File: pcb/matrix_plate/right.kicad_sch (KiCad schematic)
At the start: 39 parts

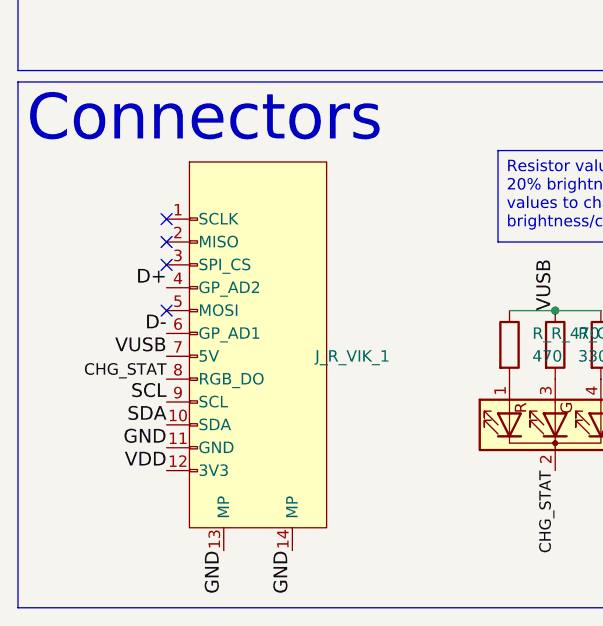
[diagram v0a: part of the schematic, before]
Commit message: Update KiCAD projects to use new library locations.
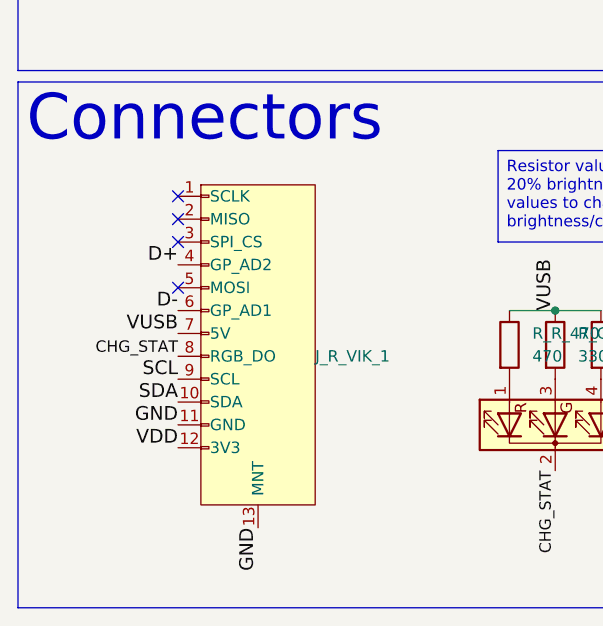
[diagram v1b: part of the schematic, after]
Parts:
- J_R_VIK_1: footprint vik:vik-module-connector-horizontal -> footprints:vik-module-connector-horizontal
- S_R_00, S_R_01, S_R_02, S_R_03, S_R_04, S_R_10, S_R_11, S_R_12, S_R_13, S_R_14, S_R_15, S_R_20, S_R_21, S_R_22, S_R_23, S_R_24, S_R_25, S_R_31, S_R_32, S_R_33, S_R_34, S_R_35: footprint key-switches:SW_GLP_Kailh_Choc_V1V2_HotSwap_PTH -> footprints:SW_GLP_Kailh_Choc_V1V2_HotSwap_PTH
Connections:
- net GND: no longer J_R_VIK_1.14 (MP)
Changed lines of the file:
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@@
 	)
 	(no_connect
-		(at 29.21 180.34)
+		(at 30.48 177.8)
 	)
 	(no_connect
@@
 	)
 	(no_connect
-		(at 29.21 187.96)
+		(at 30.48 185.42)
 	)
 	(no_connect
@@
 	)
 	(no_connect
-		(at 29.21 177.8)
+		(at 30.48 175.26)
 	)
 	(no_connect
@@
 	)
 	(no_connect
-		(at 29.21 182.88)
+		(at 30.48 180.34)
 	)
 	(wire
@@
 	)
 	(label "D+"
-		(at 29.21 185.42 180)
+		(at 30.48 182.88 180)
 		(effects
 			(font
@@
 	)
 	(label "CHG_STAT"
-		(at 29.21 195.58 180)
+		(at 30.48 193.04 180)
 		(effects
 			(font
@@
 	)
 	(label "SDA"
-		(at 29.21 200.66 180)
+		(at 30.48 198.12 180)
 		(effects
 			(font
@@
 	)
 	(label "VUSB"
-		(at 29.21 193.04 180)
+		(at 30.48 190.5 180)
 		(effects
 			(font
@@
 	)
 	(label "GND"
-		(at 29.21 203.2 180)
+		(at 30.48 200.66 180)
 		(effects
 			(font
@@
 	)
 	(label "GND"
-		(at 35.56 214.63 270)
+		(at 39.37 212.09 270)
 		(effects
 			(font
@@
 		)
 	)
-	(label "GND"
-		(at 43.18 214.63 270)
-		(effects
-			(font
-				(size 1.524 1.524)
-			)
-			(justify right bottom)
-		)
-	)
 	(label "D-"
 		(at 308.61 45.72 0)
@@
 	)
 	(label "VDD"
-		(at 29.21 205.74 180)
+		(at 30.48 203.2 180)
 		(effects
 			(font
@@
 	)
 	(label "SCL"
-		(at 29.21 198.12 180)
+		(at 30.48 195.58 180)
 		(effects
 			(font
@@
 	)
 	(label "D-"
-		(at 29.21 190.5 180)
+		(at 30.48 187.96 180)
 		(effects
 			(font
@@
 			)
 		)
-		(property "Footprint" "key-switches:SW_GLP_Kailh_Choc_V1V2_HotSwap_PTH"
+		(property "Footprint" "footprints:SW_GLP_Kailh_Choc_V1V2_HotSwap_PTH"
 			(at 207.01 69.85 0)
 			(hide yes)
@@
 			)
 		)
-		(property "Footprint" "key-switches:SW_GLP_Kailh_Choc_V1V2_HotSwap_PTH"
+		(property "Footprint" "footprints:SW_GLP_Kailh_Choc_V1V2_HotSwap_PTH"
 			(at 189.23 38.1 0)
 			(hide yes)
@@
 			)
 		)
-		(property "Footprint" "key-switches:SW_GLP_Kailh_Choc_V1V2_HotSwap_PTH"
+		(property "Footprint" "footprints:SW_GLP_Kailh_Choc_V1V2_HotSwap_PTH"
 			(at 242.57 85.09 0)
 			(hide yes)
@@
 			)
 		)
-		(property "Footprint" "vik:vik-module-connector-horizontal"
-			(at 39.37 185.42 0)
+		(property "Footprint" "footprints:vik-module-connector-horizontal"
+			(at 38.1 181.61 0)
 			(hide yes)
 			(show_name no)
@@
 		)
 		(property "Datasheet" ""
-			(at 39.37 185.42 0)
+			(at 38.1 181.61 0)
 			(hide yes)
 			(show_name no)
@@
 		)
 		(property "Description" "VIK_IN_INTC"
-			(at 50.8 195.834 0)
+			(at 38.1 187.96 0)
 			(hide yes)
 			(show_name no)
@@
 		(pin "13"
 		)
-		(pin "14"
-		)
 		(instances
 			(project "matrix_plate"
@@
 			)
 		)
-		(property "Footprint" "key-switches:SW_GLP_Kailh_Choc_V1V2_HotSwap_PTH"
+		(property "Footprint" "footprints:SW_GLP_Kailh_Choc_V1V2_HotSwap_PTH"
 			(at 242.57 53.34 0)
 			(hide yes)
@@
 			)
 		)
-		(property "Footprint" "key-switches:SW_GLP_Kailh_Choc_V1V2_HotSwap_PTH"
+		(property "Footprint" "footprints:SW_GLP_Kailh_Choc_V1V2_HotSwap_PTH"
 			(at 189.23 69.85 0)
 			(hide yes)
@@
 			)
 		)
-		(property "Footprint" "key-switches:SW_GLP_Kailh_Choc_V1V2_HotSwap_PTH"
+		(property "Footprint" "footprints:SW_GLP_Kailh_Choc_V1V2_HotSwap_PTH"
 			(at 189.23 53.34 0)
 			(hide yes)
@@
 			)
 		)
-		(property "Footprint" "key-switches:SW_GLP_Kailh_Choc_V1V2_HotSwap_PTH"
+		(property "Footprint" "footprints:SW_GLP_Kailh_Choc_V1V2_HotSwap_PTH"
 			(at 207.01 53.34 0)
 			(hide yes)
@@
 			)
 		)
-		(property "Footprint" "key-switches:SW_GLP_Kailh_Choc_V1V2_HotSwap_PTH"
+		(property "Footprint" "footprints:SW_GLP_Kailh_Choc_V1V2_HotSwap_PTH"
 			(at 171.45 53.34 0)
 			(hide yes)
@@
 			)
 		)
-		(property "Footprint" "key-switches:SW_GLP_Kailh_Choc_V1V2_HotSwap_PTH"
+		(property "Footprint" "footprints:SW_GLP_Kailh_Choc_V1V2_HotSwap_PTH"
 			(at 171.45 69.85 0)
 			(hide yes)
@@
 			)
 		)
-		(property "Footprint" "key-switches:SW_GLP_Kailh_Choc_V1V2_HotSwap_PTH"
+		(property "Footprint" "footprints:SW_GLP_Kailh_Choc_V1V2_HotSwap_PTH"
 			(at 189.23 85.09 0)
 			(hide yes)
@@
 			)
 		)
-		(property "Footprint" "key-switches:SW_GLP_Kailh_Choc_V1V2_HotSwap_PTH"
+		(property "Footprint" "footprints:SW_GLP_Kailh_Choc_V1V2_HotSwap_PTH"
 			(at 224.79 69.85 0)
 			(hide yes)
@@
 			)
 		)
-		(property "Footprint" "key-switches:SW_GLP_Kailh_Choc_V1V2_HotSwap_PTH"
+		(property "Footprint" "footprints:SW_GLP_Kailh_Choc_V1V2_HotSwap_PTH"
 			(at 224.79 53.34 0)
 			(hide yes)
@@
 			)
 		)
-		(property "Footprint" "key-switches:SW_GLP_Kailh_Choc_V1V2_HotSwap_PTH"
+		(property "Footprint" "footprints:SW_GLP_Kailh_Choc_V1V2_HotSwap_PTH"
 			(at 153.67 53.34 0)
 			(hide yes)
@@
 			)
 		)
-		(property "Footprint" "key-switches:SW_GLP_Kailh_Choc_V1V2_HotSwap_PTH"
+		(property "Footprint" "footprints:SW_GLP_Kailh_Choc_V1V2_HotSwap_PTH"
 			(at 207.01 85.09 0)
 			(hide yes)
@@
 			)
 		)
-		(property "Footprint" "key-switches:SW_GLP_Kailh_Choc_V1V2_HotSwap_PTH"
+		(property "Footprint" "footprints:SW_GLP_Kailh_Choc_V1V2_HotSwap_PTH"
 			(at 153.67 69.85 0)
 			(hide yes)
@@
 			)
 		)
-		(property "Footprint" "key-switches:SW_GLP_Kailh_Choc_V1V2_HotSwap_PTH"
+		(property "Footprint" "footprints:SW_GLP_Kailh_Choc_V1V2_HotSwap_PTH"
 			(at 224.79 85.09 0)
 			(hide yes)
@@
 			)
 		)
-		(property "Footprint" "key-switches:SW_GLP_Kailh_Choc_V1V2_HotSwap_PTH"
+		(property "Footprint" "footprints:SW_GLP_Kailh_Choc_V1V2_HotSwap_PTH"
 			(at 171.45 38.1 0)
 			(hide yes)
@@
 			)
 		)
-		(property "Footprint" "key-switches:SW_GLP_Kailh_Choc_V1V2_HotSwap_PTH"
+		(property "Footprint" "footprints:SW_GLP_Kailh_Choc_V1V2_HotSwap_PTH"
 			(at 207.01 38.1 0)
 			(hide yes)
@@
 			)
 		)
-		(property "Footprint" "key-switches:SW_GLP_Kailh_Choc_V1V2_HotSwap_PTH"
+		(property "Footprint" "footprints:SW_GLP_Kailh_Choc_V1V2_HotSwap_PTH"
 			(at 224.79 38.1 0)
 			(hide yes)
@@
 			)
 		)
-		(property "Footprint" "key-switches:SW_GLP_Kailh_Choc_V1V2_HotSwap_PTH"
+		(property "Footprint" "footprints:SW_GLP_Kailh_Choc_V1V2_HotSwap_PTH"
 			(at 153.67 38.1 0)
 			(hide yes)
@@
 			)
 		)
-		(property "Footprint" "key-switches:SW_GLP_Kailh_Choc_V1V2_HotSwap_PTH"
+		(property "Footprint" "footprints:SW_GLP_Kailh_Choc_V1V2_HotSwap_PTH"
 			(at 242.57 69.85 0)
 			(hide yes)
@@
 			)
 		)
-		(property "Footprint" "key-switches:SW_GLP_Kailh_Choc_V1V2_HotSwap_PTH"
+		(property "Footprint" "footprints:SW_GLP_Kailh_Choc_V1V2_HotSwap_PTH"
 			(at 171.45 85.09 0)
 			(hide yes)
